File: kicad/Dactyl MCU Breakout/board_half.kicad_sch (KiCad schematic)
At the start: 34 parts, among them J201 Bat, J202 Split, J203 Column, J204 Thumb, J205 External, J206 Row, J207 Display, J208 Vic, SW201 Battery, SW202 Reset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

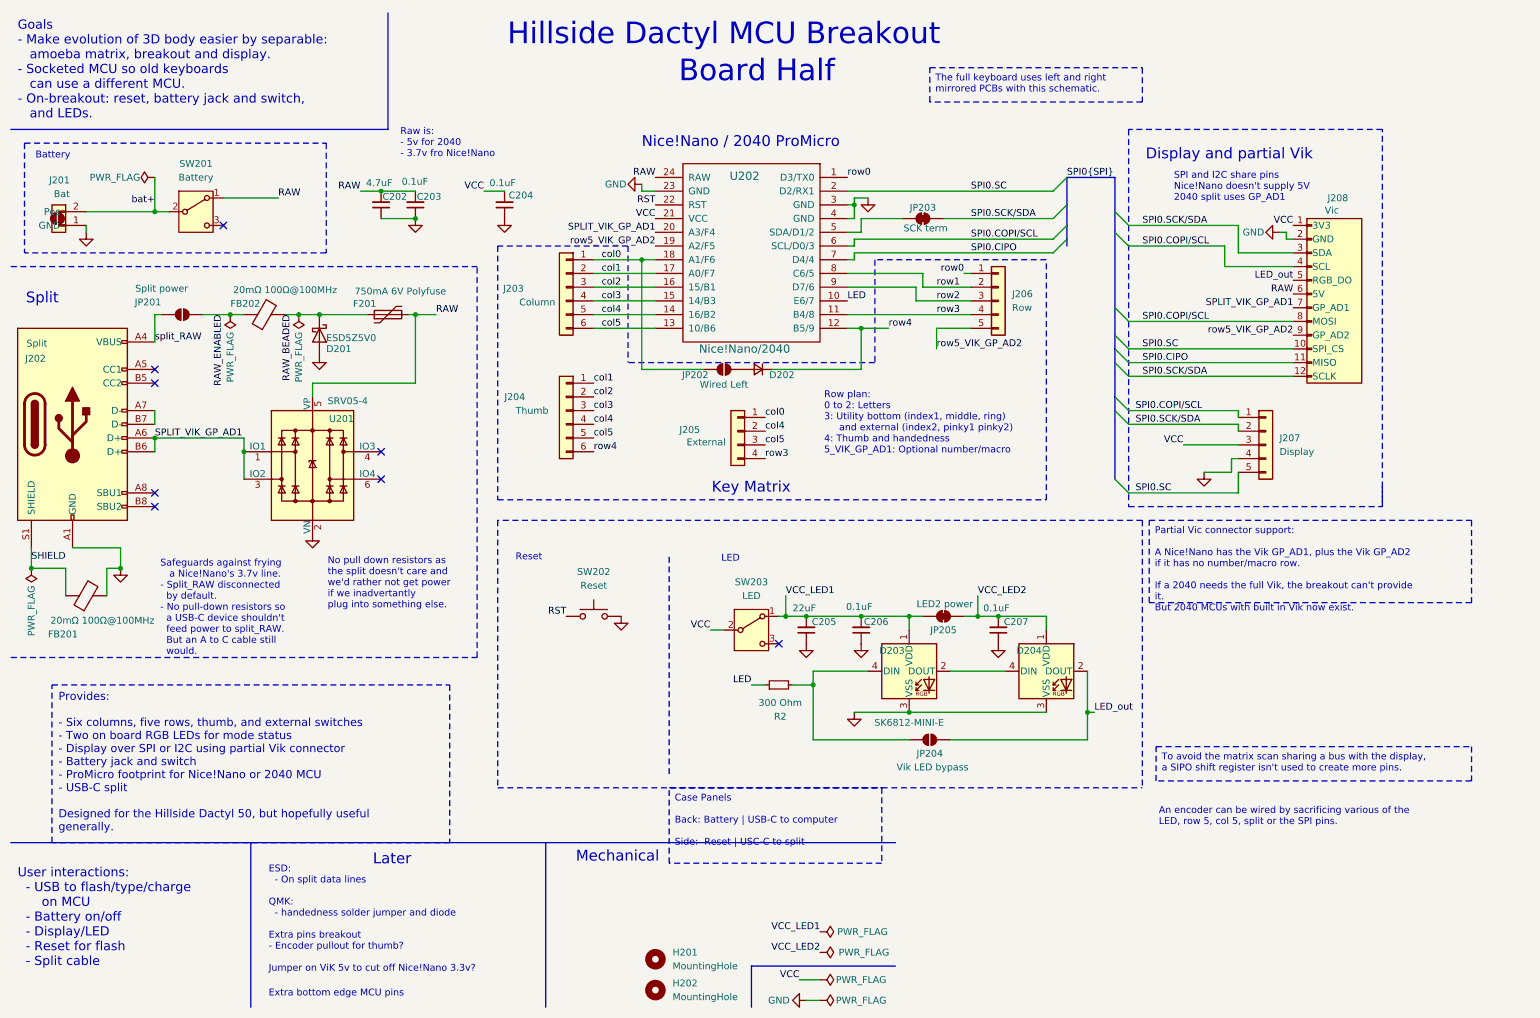
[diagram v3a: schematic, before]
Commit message: feat: simplify battery JST to one sided
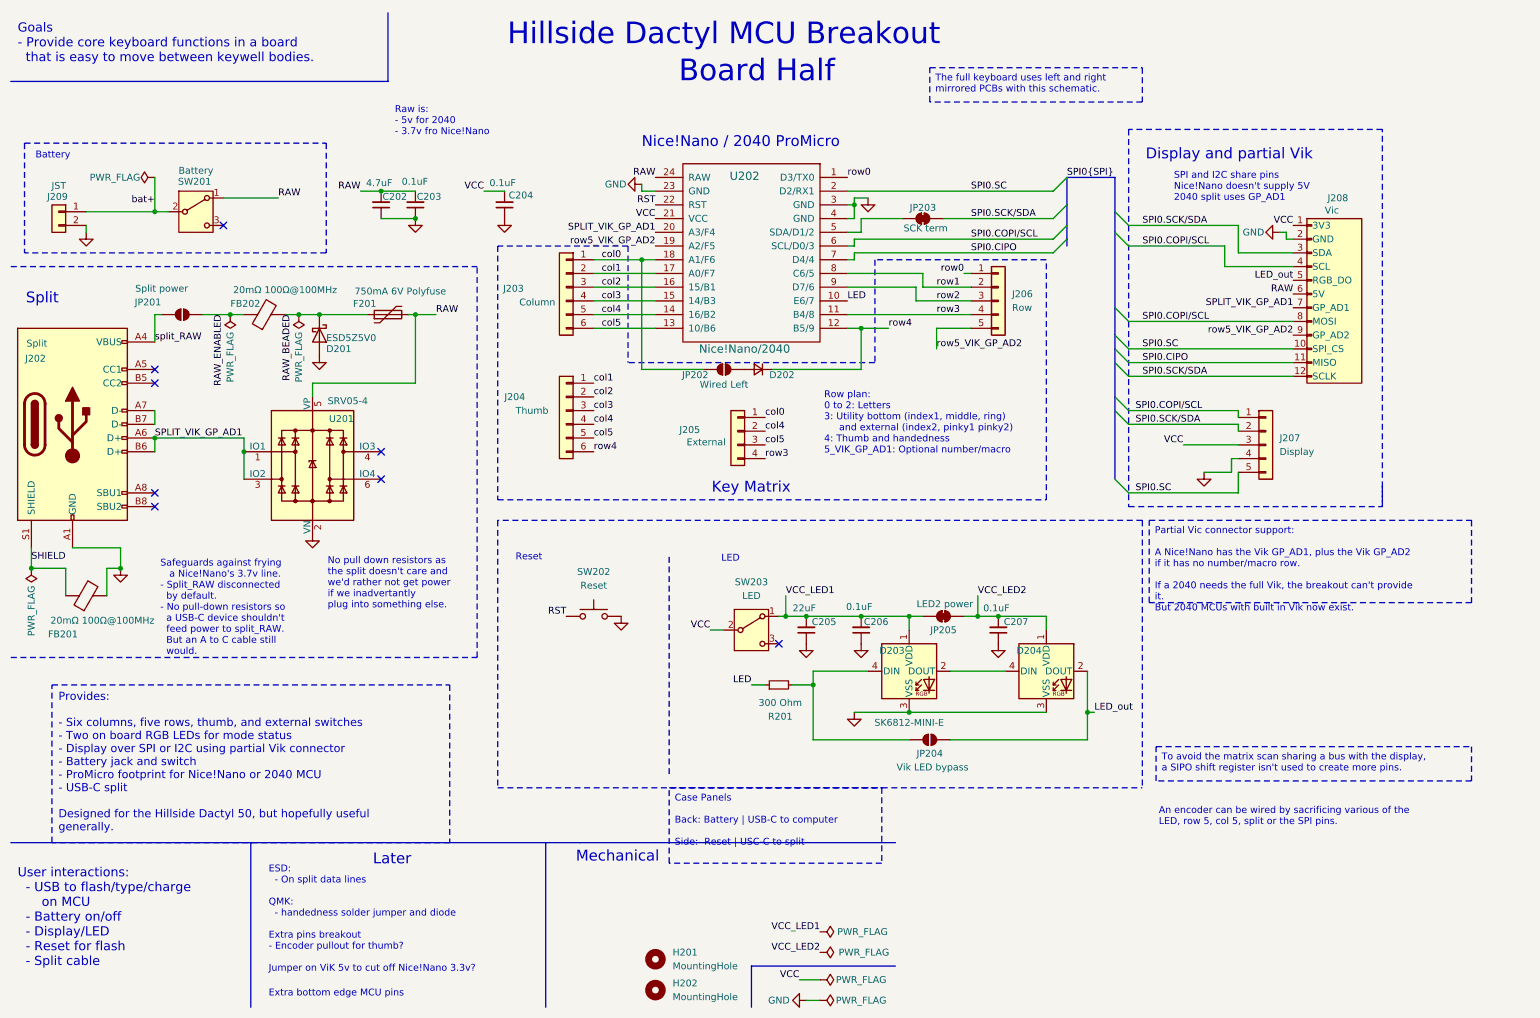
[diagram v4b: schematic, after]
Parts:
- removed J201: Bat, Dactyl:JST_PH_S2B-PH-K_1x02_P2.00mm_Horizontal, symbol Dactyl:Conn_01x02_Jump_Two_Side
- added J209: JST, Dactyl:JST_PH_S2B-PH-K_1x02_P2.00mm_Horizontal, symbol Connector_Generic:Conn_01x02
- renumbered R2 to R201
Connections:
- net GND: now also J209.2 (Pin_2)
- net bat+: now also J209.1 (Pin_1)
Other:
- note added: "Goals - Provide core keyboard functions in a board that is easy to move between keywell bodies."
- note removed: "Goals - Make evolution of 3D body easier by separable: amoeba matrix, breakout and display. - Socketed MCU so old keyboards can use a different MCU. - On-breakout: reset, battery jack and switch, and LEDs."
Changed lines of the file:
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@@
 		)
 	)
-	(wire
-		(pts
-			(xy 26.67 52.07) (xy 26.67 53.34)
-		)
-		(stroke
-			(width 0)
-			(type default)
-		)
-	)
 	(polyline
 		(pts
@@
 	(polyline
 		(pts
-			(xy 82.55 34.29) (xy 82.55 12.7)
+			(xy 82.55 25.4) (xy 82.55 12.7)
 		)
 		(stroke
@@
 	(wire
 		(pts
+			(xy 26.67 52.07) (xy 26.67 53.34)
+		)
+		(stroke
+			(width 0)
+			(type default)
+		)
+	)
+	(wire
+		(pts
 			(xy 161.29 147.32) (xy 161.29 137.16)
 		)
@@
 	(polyline
 		(pts
-			(xy 12.7 34.29) (xy 82.55 34.29)
+			(xy 12.7 25.4) (xy 82.55 25.4)
 		)
 		(stroke
@@
 		)
 	)
-	(text "Goals\n- Make evolution of 3D body easier by separable:\n   amoeba matrix, breakout and display.\n- Socketed MCU so old keyboards \n   can use a different MCU.\n- On-breakout: reset, battery jack and switch, \n   and LEDs."
+	(text "Goals\n- Provide core keyboard functions in a board \n  that is easy to move between keywell bodies."
 		(exclude_from_sim no)
-		(at 13.97 32.512 0)
+		(at 13.97 22.098 0)
 		(effects
 			(font
@@
 	(text "Raw is:\n- 5v for 2040\n- 3.7v fro Nice!Nano"
 		(exclude_from_sim no)
-		(at 84.836 39.624 0)
+		(at 83.82 35.56 0)
 		(effects
 			(font
@@
 		(dnp no)
 		(property "Reference" "SW201"
-			(at 46.99 40.64 0)
+			(at 46.736 43.942 0)
 			(effects
 				(font
@@
 		)
 		(property "Value" "Battery"
-			(at 46.99 43.18 0)
+			(at 46.99 41.91 0)
 			(effects
 				(font
@@
 		(on_board yes)
 		(dnp no)
-		(property "Reference" "R2"
+		(property "Reference" "R201"
 			(at 155.194 143.002 90)
 			(effects
@@
 	)
 	(symbol
+		(lib_id "Connector_Generic:Conn_01x02")
+		(at 21.59 49.53 0)
+		(mirror y)
+		(unit 1)
+		(exclude_from_sim no)
+		(in_bom yes)
+		(on_board yes)
+		(dnp no)
+		(property "Reference" "J209"
+			(at 21.336 46.736 0)
+			(effects
+				(font
+					(size 1.27 1.27)
+				)
+			)
+		)
+		(property "Value" "JST"
+			(at 21.59 44.704 0)
+			(effects
+				(font
+					(size 1.27 1.27)
+				)
+			)
+		)
+		(property "Footprint" "Dactyl:JST_PH_S2B-PH-K_1x02_P2.00mm_Horizontal"
+			(at 21.59 49.53 0)
+			(effects
+				(font
+					(size 1.27 1.27)
+				)
+				(hide yes)
+			)
+		)
+		(property "Datasheet" "~"
+			(at 21.59 49.53 0)
+			(effects
+				(font
+					(size 1.27 1.27)
+				)
+				(hide yes)
+			)
+		)
+		(property "Description" "Generic connector, single row, 01x02, script generated (kicad-library-utils/schlib/autogen/connector/)"
+			(at 21.59 49.53 0)
+			(effects
+				(font
+					(size 1.27 1.27)
+				)
+				(hide yes)
+			)
+		)
+		(pin "2"
+		)
+		(pin "1"
+		)
+		(instances
+			(project ""
+				(path "/454146f1-d25e-490f-a0db-4f993607d919/e235f658-1906-464a-832e-0ac06e788394"
+					(reference "J209")
+					(unit 1)
+				)
+			)
+		)
+	)
+	(symbol
 		(lib_id "Connector_Generic:Conn_01x05")
 		(at 195.58 66.04 0)
@@
 					(unit 1)
 				)
-			)
-		)
-	)
-	(symbol
-		(lib_id "Dactyl:Conn_01x02_Jump_Two_Side")
-		(at 21.59 49.53 0)
-		(mirror y)
-		(unit 1)
-		(exclude_from_sim no)
-		(in_bom yes)
-		(on_board yes)
-		(dnp no)
-		(property "Reference" "J201"
-			(at 23.622 43.688 0)
-			(effects
-				(font
-					(size 1.27 1.27)
-				)
-				(justify left)
-			)
-		)
-		(property "Value" "Bat"
-			(at 23.622 46.228 0)
-			(effects
-				(font
-					(size 1.27 1.27)
-				)
-				(justify left)
-			)
-		)
-		(property "Footprint" "Dactyl:JST_PH_S2B-PH-K_1x02_P2.00mm_Horizontal"
-			(at 19.05 57.15 0)
-			(effects
-				(font
-					(size 1.27 1.27)
-				)
-				(hide yes)
-			)
-		)
-		(property "Datasheet" "~"
-			(at 21.59 49.53 0)
-			(effects
-				(font
-					(size 1.27 1.27)
-				)
-				(hide yes)
-			)
-		)
-		(property "Description" "Generic connector, single row, 01x02, script generated (kicad-library-utils/schlib/autogen/connector/)"
-			(at 21.844 59.944 0)
-			(effects
-				(font
-					(size 1.27 1.27)
-				)
-				(hide yes)
-			)
-		)
-		(property "Config" ""
-			(at 21.59 49.53 0)
-			(effects
-				(font
-					(size 1.27 1.27)
-				)
-				(hide yes)
-			)
-		)
-		(pin "2"
-		)
-		(pin "1"
-		)
-		(pin "3"
-		)
-		(pin "4"
-		)
-		(instances
-			(project "Dactyl MCU Breakout"
-				(path "/454146f1-d25e-490f-a0db-4f993607d919/e235f658-1906-464a-832e-0ac06e788394"
-					(reference "J201")
-					(unit 1)
-				)

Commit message: feat(PCBA): add parts numbers for ESD and diode
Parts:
- C202, C203, C204, C205, C206, C207: JLC PCBA Type (none) -> Economic
- D202: footprint Dactyl_basics:D_0603_1608Metric -> Diode_SMD:D_SOD-323; JLC PCBA Type (none) -> Economic; LCSC Part (none) -> C2128
- J209: Config (none) -> DNF
- U201: JLC PCBA Type (none) -> Economic; LCSC Part (none) -> C20615829
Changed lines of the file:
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@@
 			)
 		)
-		(property "Footprint" "Dactyl_basics:D_0603_1608Metric"
+		(property "Footprint" "Diode_SMD:D_SOD-323"
 			(at 151.13 78.74 90)
 			(effects
@@
 			)
 		)
+		(property "JLC PCBA Type" "Economic"
+			(at 151.13 78.74 0)
+			(effects
+				(font
+					(size 1.27 1.27)
+				)
+				(hide yes)
+			)
+		)
+		(property "LCSC Part" "C2128"
+			(at 151.13 78.74 0)
+			(effects
+				(font
+					(size 1.27 1.27)
+				)
+				(hide yes)
+			)
+		)
 		(pin "2"
 		)
@@
 			)
 		)
+		(property "JLC PCBA Type" "Economic"
+			(at 87.63 48.26 0)
+			(effects
+				(font
+					(size 1.27 1.27)
+				)
+				(hide yes)
+			)
+		)
 		(pin "2"
 		)
@@
 			)
 		)
+		(property "Config" "DNF"
+			(at 21.59 49.53 0)
+			(effects
+				(font
+					(size 1.27 1.27)
+				)
+				(hide yes)
+			)
+		)
 		(pin "2"
 		)
@@
 			)
 		)
+		(property "JLC PCBA Type" "Economic"
+			(at 104.14 48.26 0)
+			(effects
+				(font
+					(size 1.27 1.27)
+				)
+				(hide yes)
+			)
+		)
 		(pin "2"
 		)
@@
 			)
 		)
+		(property "JLC PCBA Type" "Economic"
+			(at 68.58 96.52 0)
+			(effects
+				(font
+					(size 1.27 1.27)
+				)
+				(hide yes)
+			)
+		)
+		(property "LCSC Part" "C20615829"
+			(at 68.58 96.52 0)
+			(effects
+				(font
+					(size 1.27 1.27)
+				)
+				(hide yes)
+			)
+		)
 		(pin "2"
 		)
@@
 			)
 		)
+		(property "JLC PCBA Type" "Economic"
+			(at 195.58 127 0)
+			(effects
+				(font
+					(size 1.27 1.27)
+				)
+				(hide yes)
+			)
+		)
 		(pin "2"
 		)
@@
 			)
 		)
+		(property "JLC PCBA Type" "Economic"
+			(at 160.02 127 0)
+			(effects
+				(font
+					(size 1.27 1.27)
+				)
+				(hide yes)
+			)
+		)
 		(pin "2"
 		)
@@
 			)
 		)
+		(property "JLC PCBA Type" "Economic"
+			(at 81.28 48.26 0)
+			(effects
+				(font
+					(size 1.27 1.27)
+				)
+				(hide yes)
+			)
+		)
 		(pin "2"
 		)
@@
 			(at 170.18 127 0)
 			(effects
+				(font
+					(size 1.27 1.27)
+				)
+				(hide yes)
+			)
+		)
+		(property "JLC PCBA Type" "Economic"
+			(at 170.18 127 0)
+			(effects

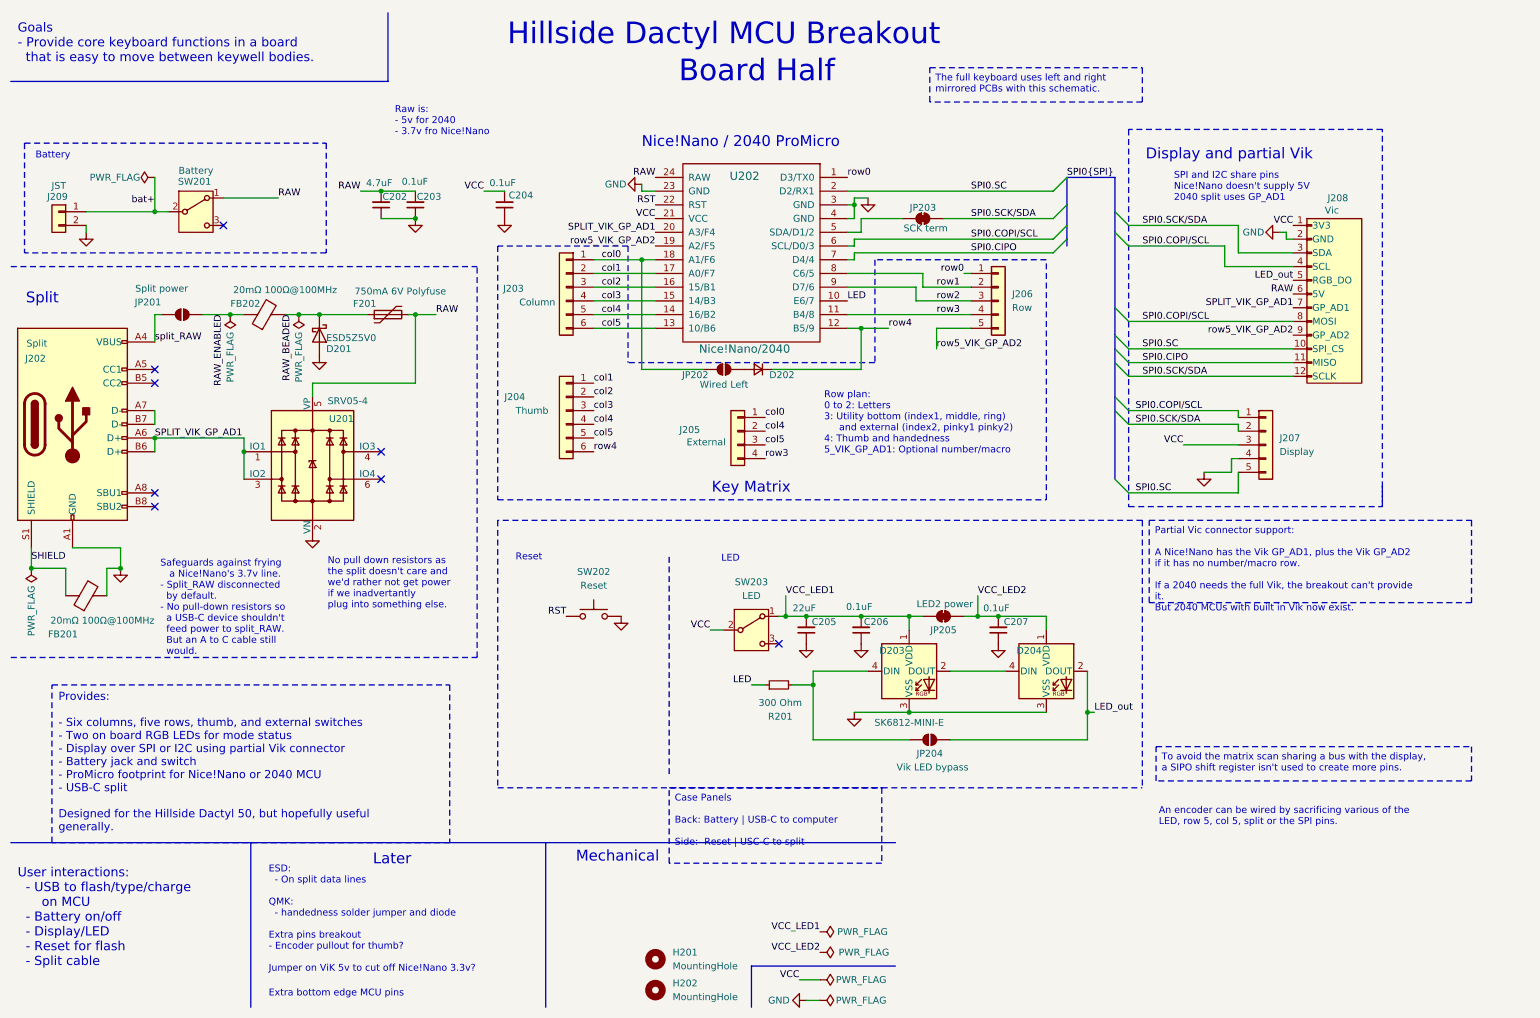
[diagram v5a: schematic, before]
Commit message: feat: cleanup routes, add role to components
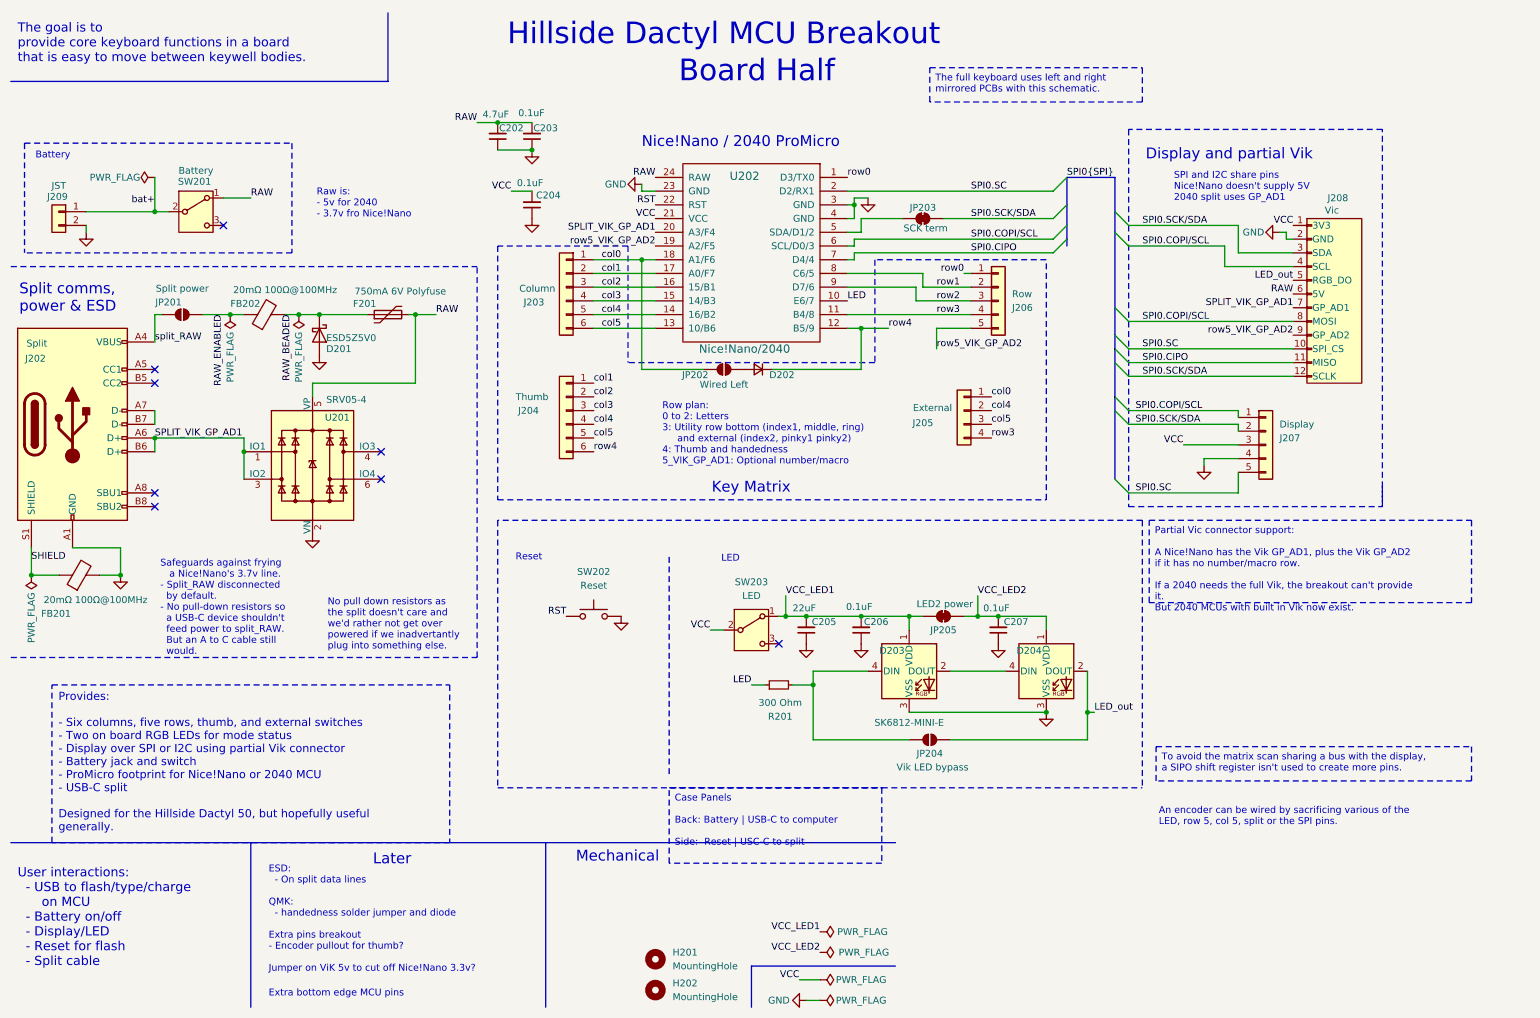
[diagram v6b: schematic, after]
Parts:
- C202, C203, C204, C205, C206, C207: JLC PCBA Type Economic -> Econom; Role (none) -> ESD basic
- D201, F201, FB201, FB202: JLC PCBA Type Economic -> Extended; Role (none) -> ESD
- D202: JLC PCBA Type Economic -> Econom; Role (none) -> Split
- D203, D204, SW203: Role (none) -> LED
- J202: JLC PCBA Type Economic -> Extended; Role (none) -> Split
- J208: JLC PCBA Type Economic -> Extended; Role (none) -> Vic
- J209: Role (none) -> Battery
- R201: JLC PCBA Type (none) -> Econom; Role (none) -> LED
- SW201: Role (none) -> Batt
- SW202: Role (none) -> Reset
- U201: JLC PCBA Type Economic -> Extended Prefer; Role (none) -> ESD
- U202: Role (none) -> MCU
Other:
- note added: "No pull down resistors as the split doesn't care and we'd rather not get over powered if we inadvertantly plug into something else."
- note added: "Row plan: 0 to 2: Letters 3: Utility row bottom (index1, middle, ring) and external (index2, pinky1 pinky2) 4: Thumb and handedness 5_VIK_GP_AD1: Optional number/macro"
- note added: "The goal is to provide core keyboard functions in a board that is easy to move between keywell bodies."
- note removed: "Goals - Provide core keyboard functions in a board that is easy to move between keywell bodies."
- note removed: "No pull down resistors as the split doesn't care and we'd rather not get power if we inadvertantly plug into something else."
- note removed: "Row plan: 0 to 2: Letters 3: Utility bottom (index1, middle, ring) and external (index2, pinky1 pinky2) 4: Thumb and handedness 5_VIK_GP_AD1: Optional number/macro"
- note removed: "Split"
- moved on the sheet: C202, C203, C204, FB201, J205

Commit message: feat: remove warn disables after update footprints
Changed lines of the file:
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@@
 	(polyline
 		(pts
-			(xy 82.55 25.4) (xy 82.55 12.7)
+			(xy 76.2 25.4) (xy 76.2 12.7)
 		)
 		(stroke
@@
 	(polyline
 		(pts
-			(xy 12.7 25.4) (xy 82.55 25.4)
-		)
-		(stroke
+			(xy 12.7 25.4) (xy 76.2 25.4)
+		)
+		(stroke

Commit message: feat(pcb): left half re-numbered and some routed
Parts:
- renumbered J209 to J301
